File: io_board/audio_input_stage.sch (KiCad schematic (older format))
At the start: 31 parts

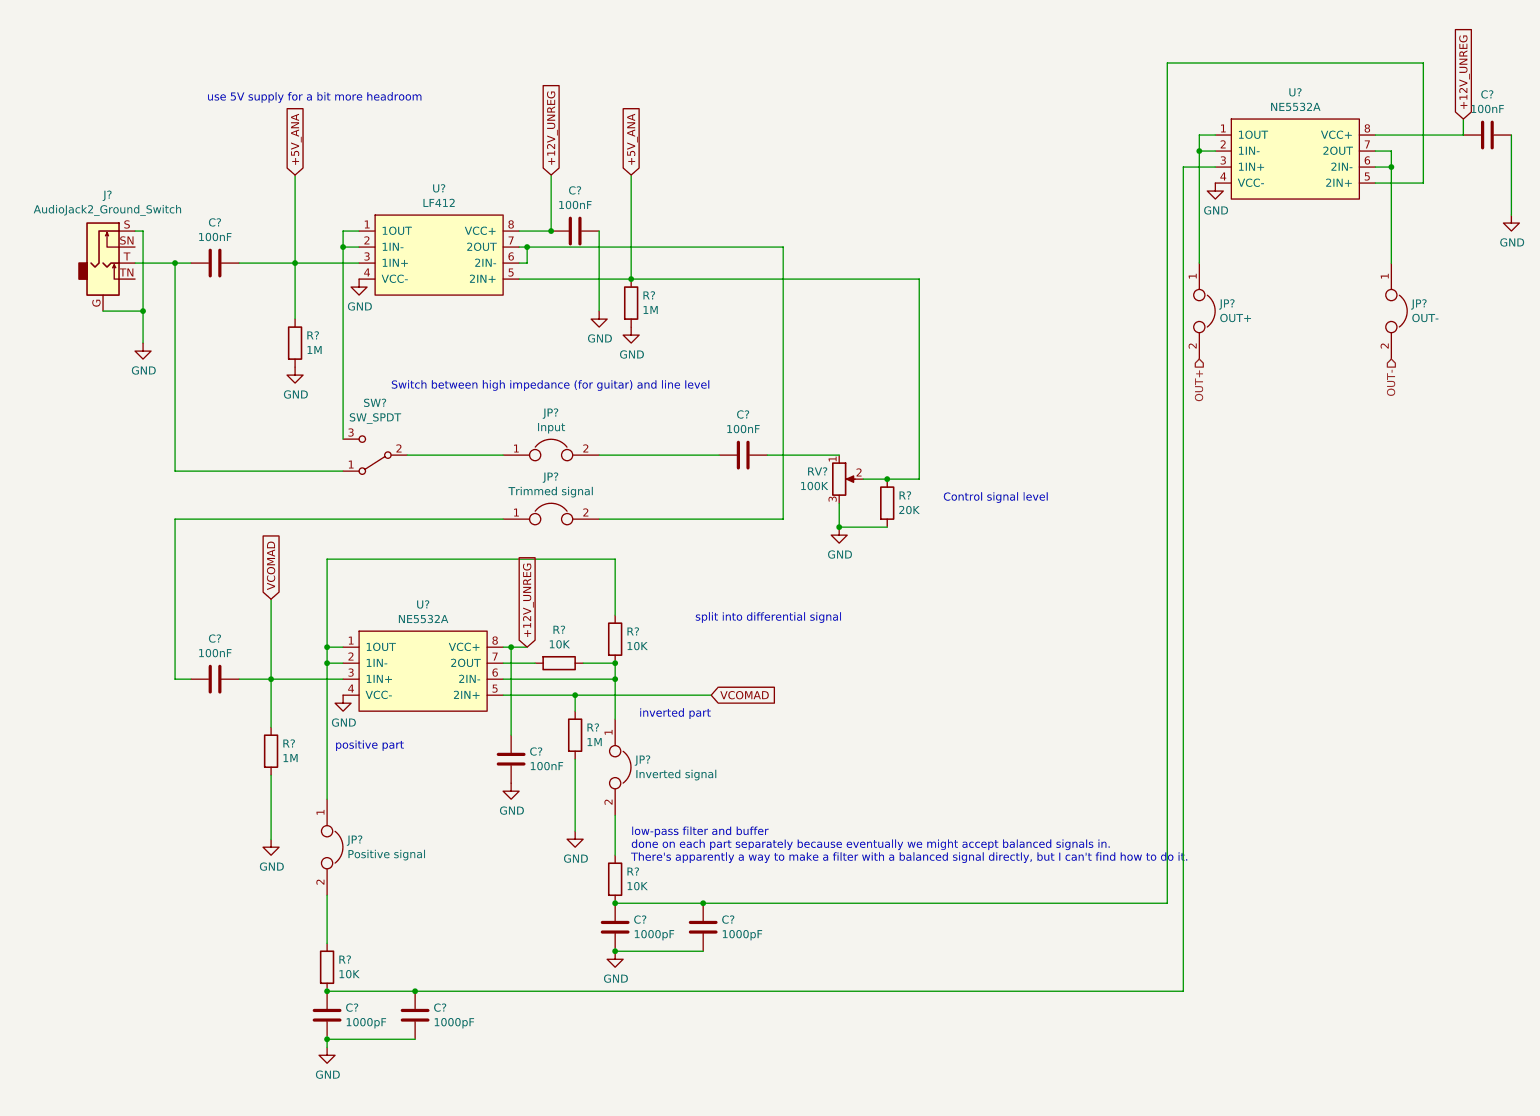
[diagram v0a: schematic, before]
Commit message: Added MIDI connectors and SD card to io_board
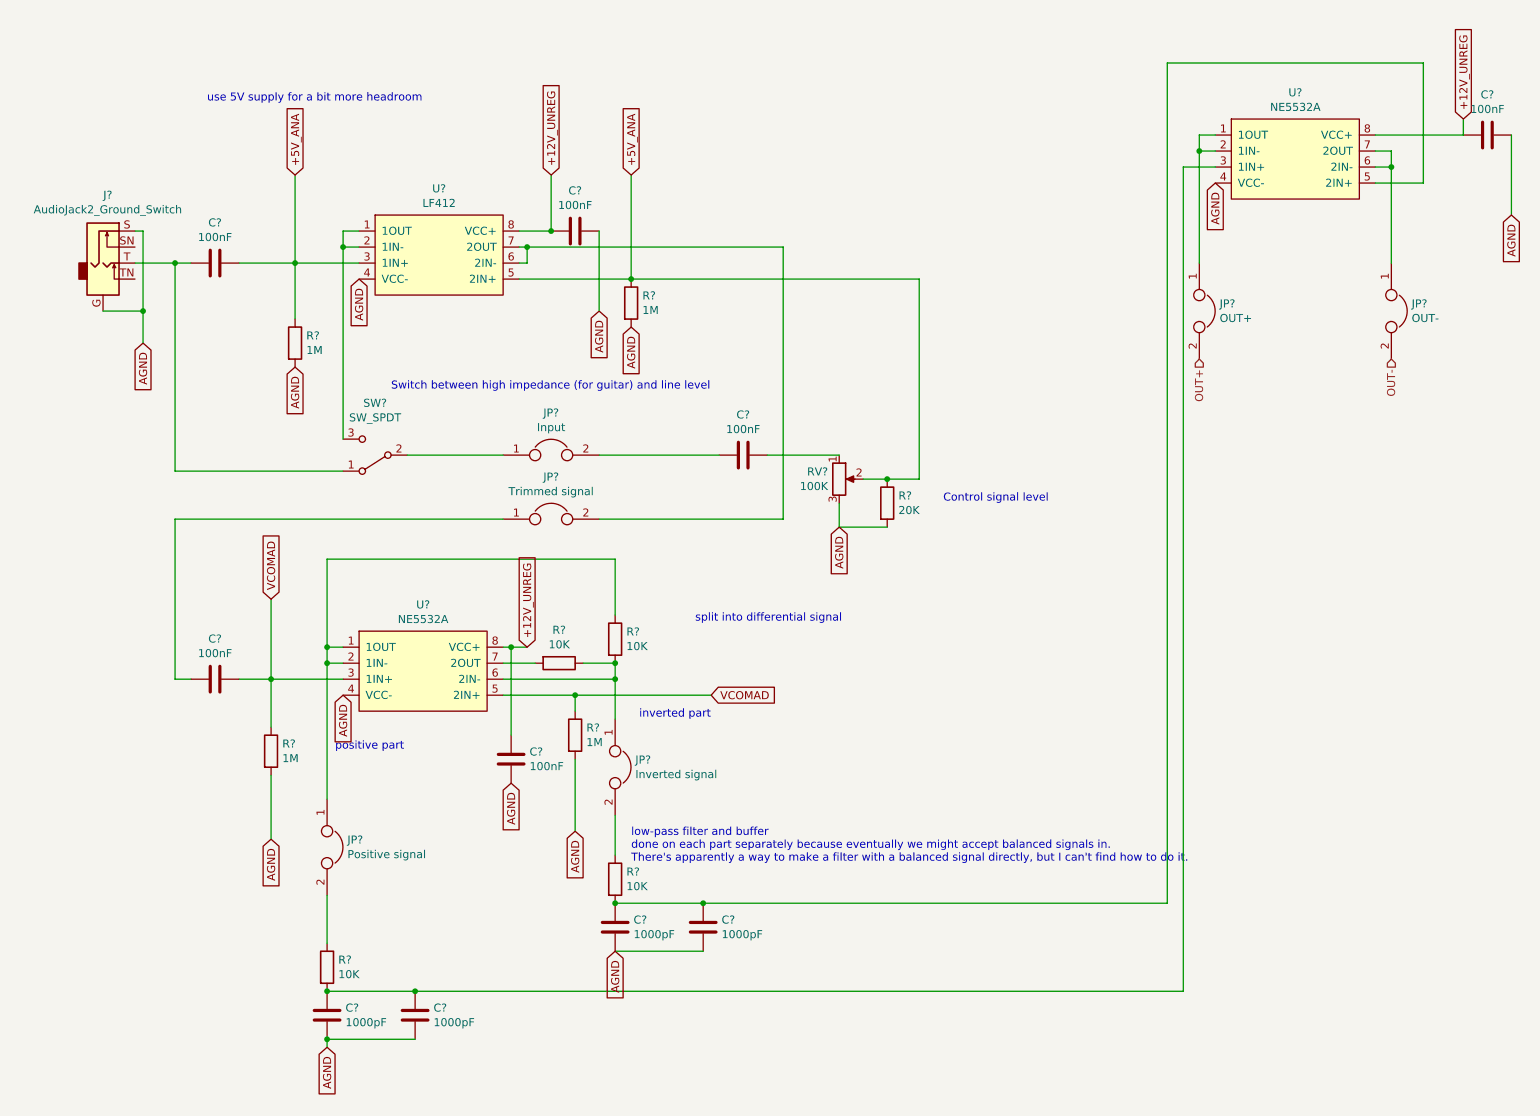
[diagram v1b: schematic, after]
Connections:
- net GND renamed AGND
